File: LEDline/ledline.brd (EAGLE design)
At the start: 160 x 100 mm, 12 parts

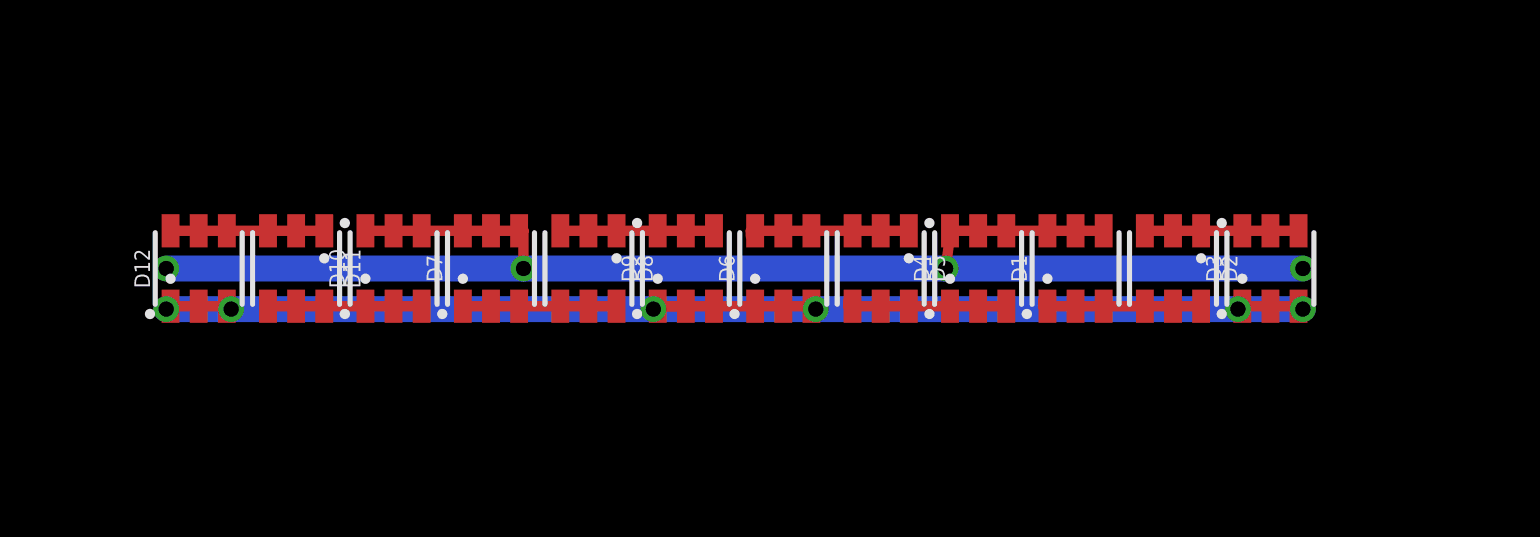
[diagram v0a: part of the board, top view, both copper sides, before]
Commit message: Heatsink and testpad added
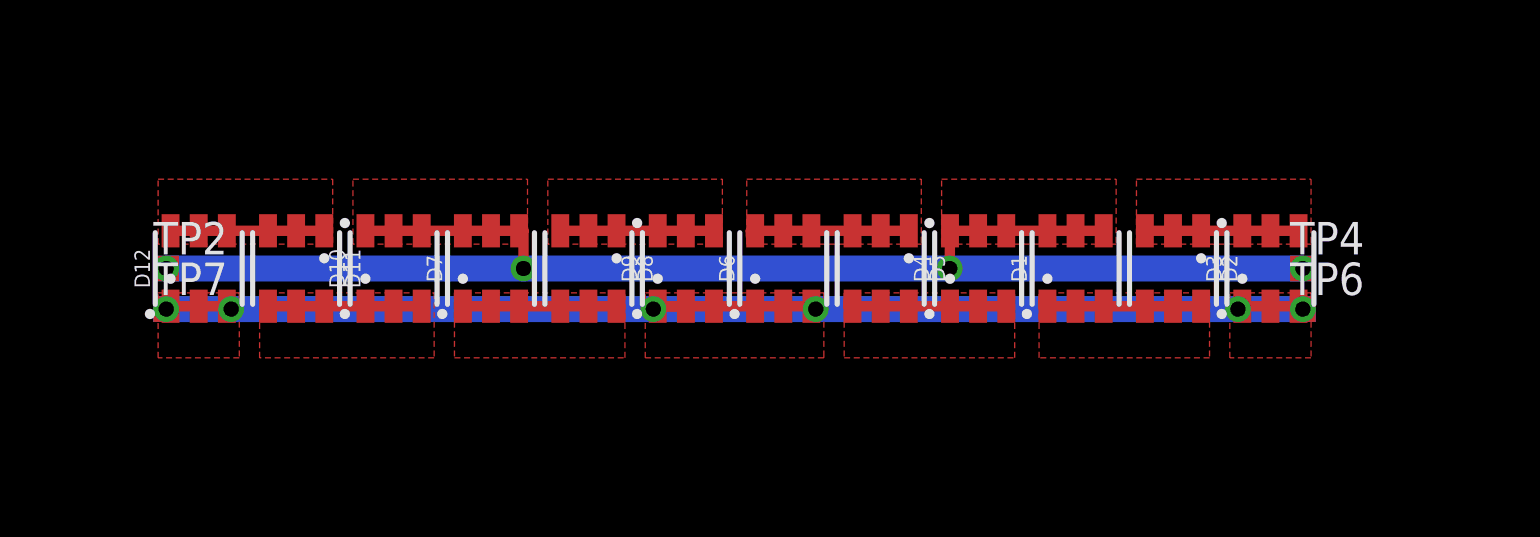
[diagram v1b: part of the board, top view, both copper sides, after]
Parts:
- added TP1, TP2, TP3, TP4, TP5, TP6, TP7, TP8: TPSQTP10SQ, testpad:TP10SQ
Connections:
- net GND: now also TP5.TP, TP6.TP, TP7.TP, TP8.TP
- net VCC: now also TP1.TP, TP2.TP, TP3.TP, TP4.TP
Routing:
- added copper zone on layer 1, net GND
- added copper zone on layer 1, net N$12
- added copper zone on layer 1, net N$13
- added copper zone on layer 1, net N$16
- added copper zone on layer 1, net N$17
- added copper zone on layer 1, net N$2
- added copper zone on layer 1, net N$4
- added copper zone on layer 1, net N$8
- added copper zone on layer 1, net N$9
- added copper zone on layer 1, net VCC
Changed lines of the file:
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@@
 <setting verticaltext="up"/>
 </settings>
-<grid distance="0.00625" unitdist="inch" unit="inch" style="lines" multiple="1" display="no" altdistance="0.025" altunitdist="inch" altunit="inch"/>
+<grid distance="0.00625" unitdist="inch" unit="mil" style="lines" multiple="1" display="no" altdistance="0.025" altunitdist="inch" altunit="inch"/>
 <layers>
 <layer number="1" name="Top" color="4" fill="1" visible="yes" active="yes"/>
@@
 <attribute name="PROD_ID" value="DIO-12113" x="46.99" y="77.47" size="1.778" layer="27" rot="R90" display="off"/>
 </element>
+<element name="TP2" library="testpad" package="TP10SQ" value="TPSQTP10SQ" x="26.67" y="77.47">
+<attribute name="TP_SIGNAL_NAME" value="" x="26.67" y="77.47" size="1.778" layer="27" display="off"/>
+</element>
+<element name="TP1" library="testpad" package="TP10SQ" value="TPSQTP10SQ" x="26.67" y="77.47" rot="MR0">
+<attribute name="TP_SIGNAL_NAME" value="" x="26.67" y="77.47" size="1.778" layer="28" rot="MR0" display="off"/>
+</element>
+<element name="TP3" library="testpad" package="TP10SQ" value="TPSQTP10SQ" x="71.12" y="77.47" rot="MR0">
+<attribute name="TP_SIGNAL_NAME" value="" x="71.12" y="77.47" size="1.778" layer="28" rot="MR0" display="off"/>
+</element>
+<element name="TP4" library="testpad" package="TP10SQ" value="TPSQTP10SQ" x="71.12" y="77.47">
+<attribute name="TP_SIGNAL_NAME" value="" x="71.12" y="77.47" size="1.778" layer="27" display="off"/>
+</element>
+<element name="TP5" library="testpad" package="TP10SQ" value="TPSQTP10SQ" x="71.12" y="75.8825" rot="MR0">
+<attribute name="TP_SIGNAL_NAME" value="" x="71.12" y="75.8825" size="1.778" layer="28" rot="MR0" display="off"/>
+</element>
+<element name="TP6" library="testpad" package="TP10SQ" value="TPSQTP10SQ" x="71.12" y="75.8825">
+<attribute name="TP_SIGNAL_NAME" value="" x="71.12" y="75.8825" size="1.778" layer="27" display="off"/>
+</element>
+<element name="TP7" library="testpad" package="TP10SQ" value="TPSQTP10SQ" x="26.67" y="75.8825">
+<attribute name="TP_SIGNAL_NAME" value="" x="26.67" y="75.8825" size="1.778" layer="27" display="off"/>
+</element>
+<element name="TP8" library="testpad" package="TP10SQ" value="TPSQTP10SQ" x="26.67" y="75.8825" rot="MR0">
+<attribute name="TP_SIGNAL_NAME" value="" x="26.67" y="75.8825" size="1.778" layer="28" rot="MR0" display="off"/>
+</element>
 </elements>
 <signals>
@@
 <wire x1="61.13" y1="75.995" x2="60.96" y2="75.995" width="0.4064" layer="1"/>
 <wire x1="60.96" y1="75.995" x2="60.96" y2="76.2" width="0.4064" layer="1"/>
+<polygon width="0.3048" layer="1" thermals="no">
+<vertex x="60.80125" y="73.9775"/>
+<vertex x="60.80125" y="76.5175"/>
+<vertex x="67.46875" y="76.5175"/>
+<vertex x="67.46875" y="73.9775"/>
+</polygon>
 </signal>
 <signal name="N$4">
@@
 <wire x1="66.04" y1="78.945" x2="67.14" y2="78.945" width="0.4064" layer="1"/>
 <wire x1="69.85" y1="78.945" x2="68.75" y2="78.945" width="0.4064" layer="1"/>
+<polygon width="0.3048" layer="1" thermals="no">
+<vertex x="64.61125" y="78.4225"/>
+<vertex x="64.61125" y="80.9625"/>
+<vertex x="71.4375" y="80.9625"/>
+<vertex x="71.4375" y="78.4225"/>
+</polygon>
 </signal>
 <signal name="N$8">
@@
 <wire x1="53.51" y1="75.995" x2="53.34" y2="75.995" width="0.4064" layer="1"/>
 <wire x1="53.34" y1="75.995" x2="53.34" y2="76.2" width="0.4064" layer="1"/>
+<polygon width="0.3048" layer="1" thermals="no">
+<vertex x="53.18125" y="76.5175"/>
+<vertex x="53.18125" y="73.9775"/>
+<vertex x="59.84875" y="73.9775"/>
+<vertex x="59.84875" y="76.5175"/>
+</polygon>
 </signal>
 <signal name="N$9">
@@
 <wire x1="49.7" y1="78.945" x2="49.53" y2="78.945" width="0.4064" layer="1"/>
 <wire x1="49.53" y1="78.945" x2="49.53" y2="78.74" width="0.4064" layer="1"/>
+<polygon width="0.3048" layer="1" thermals="no">
+<vertex x="49.37125" y="78.4225"/>
+<vertex x="49.37125" y="80.9625"/>
+<vertex x="56.1975" y="80.9625"/>
+<vertex x="56.1975" y="78.4225"/>
+</polygon>
 </signal>
 <signal name="N$12">
@@
 <wire x1="43.18" y1="75.995" x2="42.08" y2="75.995" width="0.4064" layer="1"/>
 <wire x1="39.37" y1="75.995" x2="40.47" y2="75.995" width="0.4064" layer="1"/>
+<polygon width="0.3048" layer="1" thermals="no">
+<vertex x="37.94125" y="76.5175"/>
+<vertex x="37.94125" y="73.9775"/>
+<vertex x="44.60875" y="73.9775"/>
+<vertex x="44.60875" y="76.5175"/>
+</polygon>
 </signal>
 <signal name="N$13">
@@
 <wire x1="46.99" y1="78.945" x2="48.09" y2="78.945" width="0.4064" layer="1"/>
 <wire x1="46.99" y1="78.945" x2="45.89" y2="78.945" width="0.4064" layer="1"/>
+<polygon width="0.3048" layer="1" thermals="no">
+<vertex x="41.5925" y="78.4225"/>
+<vertex x="41.5925" y="80.9625"/>
+<vertex x="48.41875" y="80.9625"/>
+<vertex x="48.41875" y="78.4225"/>
+</polygon>
 </signal>
 <signal name="N$16">
@@
 <wire x1="30.65" y1="75.995" x2="31.75" y2="75.995" width="0.4064" layer="1"/>
 <wire x1="31.75" y1="75.995" x2="31.75" y2="76.2" width="0.4064" layer="1"/>
+<polygon width="0.3048" layer="1" thermals="no">
+<vertex x="30.32125" y="73.9775"/>
+<vertex x="30.32125" y="76.5175"/>
+<vertex x="37.1475" y="76.5175"/>
+<vertex x="37.1475" y="73.9775"/>
+</polygon>
 </signal>
 <signal name="N$17">
@@
 <wire x1="32.85" y1="78.945" x2="31.75" y2="78.945" width="0.4064" layer="1"/>
 <wire x1="31.75" y1="78.945" x2="31.75" y2="78.74" width="0.4064" layer="1"/>
+<polygon width="0.3048" layer="1" thermals="no">
+<vertex x="26.3525" y="78.4225"/>
+<vertex x="26.3525" y="80.9625"/>
+<vertex x="33.17875" y="80.9625"/>
+<vertex x="33.17875" y="78.4225"/>
+</polygon>
 </signal>
 <signal name="VCC">
@@
 <wire x1="40.64" y1="78.945" x2="40.64" y2="77.47" width="0.4064" layer="1"/>
 <via x="40.64" y="77.47" extent="1-16" drill="0.6" shape="square"/>
-<wire x1="40.64" y1="77.47" x2="57.15" y2="77.47" width="1.016" layer="16"/>
-<via x="57.15" y="77.47" extent="1-16" drill="0.6" shape="square"/>
-<wire x1="57.15" y1="77.47" x2="57.32" y2="78.74" width="0.4064" layer="1"/>
+<wire x1="40.64" y1="77.47" x2="57.30875" y2="77.47" width="1.016" layer="16"/>
+<via x="57.30875" y="77.47" extent="1-16" drill="0.6" shape="square"/>
+<wire x1="57.30875" y1="77.47" x2="57.32" y2="78.74" width="0.4064" layer="1"/>
 <wire x1="57.32" y1="78.74" x2="57.32" y2="78.945" width="0.4064" layer="1"/>
 <wire x1="62.23" y1="78.945" x2="63.33" y2="78.945" width="0.4064" layer="1"/>
@@
 <wire x1="58.42" y1="78.945" x2="59.52" y2="78.945" width="0.4064" layer="1"/>
 <wire x1="40.64" y1="77.47" x2="26.67" y2="77.47" width="1.016" layer="16"/>
-<wire x1="57.15" y1="77.47" x2="71.12" y2="77.47" width="1.016" layer="16"/>
+<wire x1="57.30875" y1="77.47" x2="71.12" y2="77.47" width="1.016" layer="16"/>
 <via x="71.12" y="77.47" extent="1-16" drill="0.6" shape="square"/>
 <via x="26.67" y="77.47" extent="1-16" drill="0.6" shape="square"/>
+<contactref element="TP2" pad="TP"/>
+<contactref element="TP1" pad="TP"/>
+<contactref element="TP3" pad="TP"/>
+<contactref element="TP4" pad="TP"/>
+<polygon width="0.3048" layer="1" thermals="no">
+<vertex x="56.99125" y="78.4225"/>
+<vertex x="56.99125" y="80.9625"/>
+<vertex x="63.8175" y="80.9625"/>
+<vertex x="63.8175" y="78.4225"/>
+</polygon>
+<polygon width="0.3048" layer="1" thermals="no">
+<vertex x="33.9725" y="78.4225"/>
+<vertex x="33.9725" y="80.9625"/>
+<vertex x="40.79875" y="80.9625"/>
+<vertex x="40.79875" y="78.4225"/>
+</polygon>
 </signal>
 <signal name="GND">
@@
 <wire x1="29.21" y1="75.8825" x2="26.67" y2="75.8825" width="1.016" layer="16"/>
 <via x="26.67" y="75.8825" extent="1-16" drill="0.6" shape="square"/>
+<contactref element="TP8" pad="TP"/>
+<contactref element="TP7" pad="TP"/>
+<contactref element="TP6" pad="TP"/>
+<contactref element="TP5" pad="TP"/>
+<polygon width="0.3048" layer="1" thermals="no">
+<vertex x="26.3525" y="73.9775"/>
+<vertex x="26.3525" y="76.5175"/>
+<vertex x="29.5275" y="76.5175"/>
+<vertex x="29.5275" y="73.9775"/>
+</polygon>
+<polygon width="0.3048" layer="1" thermals="no">
+<vertex x="45.4025" y="73.9775"/>
+<vertex x="45.4025" y="76.5175"/>
+<vertex x="52.3875" y="76.5175"/>
+<vertex x="52.3875" y="74.13625"/>
+<vertex x="52.3875" y="73.9775"/>
+</polygon>
+<polygon width="0.3048" layer="1" thermals="no">
+<vertex x="68.2625" y="73.9775"/>
+<vertex x="68.2625" y="76.5175"/>
+<vertex x="71.4375" y="76.5175"/>
+<vertex x="71.4375" y="73.9775"/>
+</polygon>
 </signal>
 </signals>

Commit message: MOAAAAR heatsink
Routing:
- net VCC: track 59.6 -> 56.8 mm, vias 4 -> 6
- net N$9: vias 0 -> 2
- net N$4: vias 0 -> 2
- net N$17: vias 0 -> 2
- net N$13: vias 0 -> 2
- added copper zone on layer 16, net GND
- added copper zone on layer 16, net N$13
- added copper zone on layer 16, net N$17
- added copper zone on layer 16, net N$4
- added copper zone on layer 16, net N$9
- added copper zone on layer 16, net VCC
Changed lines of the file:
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@@
 <layer number="27" name="tValues" color="7" fill="1" visible="no" active="yes"/>
 <layer number="28" name="bValues" color="7" fill="1" visible="no" active="yes"/>
-<layer number="29" name="tStop" color="7" fill="3" visible="no" active="yes"/>
-<layer number="30" name="bStop" color="7" fill="6" visible="no" active="yes"/>
+<layer number="29" name="tStop" color="7" fill="3" visible="yes" active="yes"/>
+<layer number="30" name="bStop" color="7" fill="6" visible="yes" active="yes"/>
 <layer number="31" name="tCream" color="7" fill="4" visible="no" active="yes"/>
 <layer number="32" name="bCream" color="7" fill="5" visible="no" active="yes"/>
@@
 <wire x1="160" y1="100" x2="0" y2="100" width="0" layer="20"/>
 <wire x1="0" y1="100" x2="0" y2="0" width="0" layer="20"/>
+<polygon width="0.3048" layer="29">
+<vertex x="26.3525" y="73.9775"/>
+<vertex x="29.5275" y="73.9775"/>
+<vertex x="29.5275" y="74.93"/>
+<vertex x="26.3525" y="74.93"/>
+</polygon>
+<polygon width="0.3048" layer="30">
+<vertex x="26.3525" y="74.93"/>
+<vertex x="26.3525" y="73.9775"/>
+<vertex x="29.5275" y="73.9775"/>
+<vertex x="29.5275" y="74.93"/>
+</polygon>
+<polygon width="0.3048" layer="29">
+<vertex x="68.2625" y="73.9775"/>
+<vertex x="71.4375" y="73.9775"/>
+<vertex x="71.4375" y="74.93"/>
+<vertex x="68.2625" y="74.93"/>
+</polygon>
+<polygon width="0.3048" layer="30">
+<vertex x="68.2625" y="74.93"/>
+<vertex x="68.2625" y="73.9775"/>
+<vertex x="71.4375" y="73.9775"/>
+<vertex x="71.4375" y="74.93"/>
+</polygon>
+<polygon width="0.3048" layer="29">
+<vertex x="63.8175" y="80.9625"/>
+<vertex x="56.99125" y="80.9625"/>
+<vertex x="56.99125" y="80.16875"/>
+<vertex x="63.8175" y="80.16875"/>
+</polygon>
+<polygon width="0.3048" layer="30">
+<vertex x="56.99125" y="80.9625"/>
+<vertex x="56.99125" y="80.16875"/>
+<vertex x="63.8175" y="80.16875"/>
+<vertex x="63.8175" y="80.9625"/>
+</polygon>
+<polygon width="0.3048" layer="29">
+<vertex x="33.9725" y="80.9625"/>
+<vertex x="33.9725" y="80.16875"/>
+<vertex x="40.79875" y="80.16875"/>
+<vertex x="40.79875" y="80.9625"/>
+</polygon>
+<polygon width="0.3048" layer="30">
+<vertex x="33.9725" y="80.9625"/>
+<vertex x="33.9725" y="80.16875"/>
+<vertex x="40.79875" y="80.16875"/>
+<vertex x="40.79875" y="80.9625"/>
+</polygon>
 </plain>
 <attributes>
@@
 <vertex x="71.4375" y="78.4225"/>
 </polygon>
+<polygon width="0.3048" layer="16" thermals="no">
+<vertex x="64.61125" y="80.9625"/>
+<vertex x="64.61125" y="78.4225"/>
+<vertex x="71.4375" y="78.4225"/>
+<vertex x="71.4375" y="80.9625"/>
+</polygon>
+<via x="66.04" y="78.89875" extent="1-16" drill="0.6" shape="square"/>
+<via x="69.85" y="78.89875" extent="1-16" drill="0.6" shape="square"/>
 </signal>
 <signal name="N$8">
@@
 <vertex x="56.1975" y="78.4225"/>
 </polygon>
+<polygon width="0.3048" layer="16" thermals="no">
+<vertex x="49.37125" y="80.9625"/>
+<vertex x="56.1975" y="80.9625"/>
+<vertex x="56.1975" y="78.4225"/>
+<vertex x="49.37125" y="78.4225"/>
+</polygon>
+<via x="50.8" y="78.89875" extent="1-16" drill="0.6" shape="square"/>
+<via x="54.61" y="78.89875" extent="1-16" drill="0.6" shape="square"/>
 </signal>
 <signal name="N$12">
@@
 <vertex x="48.41875" y="78.4225"/>
 </polygon>
+<polygon width="0.3048" layer="16" thermals="no">
+<vertex x="41.5925" y="80.9625"/>
+<vertex x="41.5925" y="78.4225"/>
+<vertex x="48.41875" y="78.4225"/>
+<vertex x="48.41875" y="80.9625"/>
+</polygon>
+<via x="43.18" y="78.89875" extent="1-16" drill="0.6" shape="square"/>
+<via x="46.99" y="78.89875" extent="1-16" drill="0.6" shape="square"/>
 </signal>
 <signal name="N$16">
@@
 <wire x1="30.65" y1="78.945" x2="31.75" y2="78.945" width="0.4064" layer="1"/>
 <wire x1="32.85" y1="78.945" x2="31.75" y2="78.945" width="0.4064" layer="1"/>
-<wire x1="31.75" y1="78.945" x2="31.75" y2="78.74" width="0.4064" layer="1"/>
+<wire x1="31.75" y1="78.945" x2="31.75" y2="78.89875" width="0.4064" layer="1"/>
 <polygon width="0.3048" layer="1" thermals="no">
 <vertex x="26.3525" y="78.4225"/>
@@
 <vertex x="33.17875" y="78.4225"/>
 </polygon>
+<polygon width="0.3048" layer="16" thermals="no">
+<vertex x="26.3525" y="80.9625"/>
+<vertex x="33.17875" y="80.9625"/>
+<vertex x="33.17875" y="78.4225"/>
+<vertex x="26.3525" y="78.4225"/>
+</polygon>
+<wire x1="31.75" y1="78.89875" x2="31.75" y2="78.74" width="0.4064" layer="1"/>
+<via x="31.75" y="78.89875" extent="1-16" drill="0.6" shape="square"/>
+<via x="27.94" y="78.89875" extent="1-16" drill="0.6" shape="square"/>
 </signal>
 <signal name="VCC">
@@
 <wire x1="36.66" y1="78.945" x2="35.56" y2="78.945" width="0.4064" layer="1"/>
 <wire x1="40.47" y1="78.945" x2="40.64" y2="78.945" width="0.4064" layer="1"/>
-<wire x1="40.64" y1="78.945" x2="40.64" y2="77.47" width="0.4064" layer="1"/>
 <via x="40.64" y="77.47" extent="1-16" drill="0.6" shape="square"/>
 <wire x1="40.64" y1="77.47" x2="57.30875" y2="77.47" width="1.016" layer="16"/>
 <via x="57.30875" y="77.47" extent="1-16" drill="0.6" shape="square"/>
-<wire x1="57.30875" y1="77.47" x2="57.32" y2="78.74" width="0.4064" layer="1"/>
 <wire x1="57.32" y1="78.74" x2="57.32" y2="78.945" width="0.4064" layer="1"/>
 <wire x1="62.23" y1="78.945" x2="63.33" y2="78.945" width="0.4064" layer="1"/>
@@
 <contactref element="TP4" pad="TP"/>
 <polygon width="0.3048" layer="1" thermals="no">
-<vertex x="56.99125" y="78.4225"/>
+<vertex x="56.99125" y="77.1525"/>
 <vertex x="56.99125" y="80.9625"/>
 <vertex x="63.8175" y="80.9625"/>
-<vertex x="63.8175" y="78.4225"/>
-</polygon>
-<polygon width="0.3048" layer="1" thermals="no">
-<vertex x="33.9725" y="78.4225"/>
+<vertex x="63.8175" y="77.1525"/>
+</polygon>
+<polygon width="0.3048" layer="1" thermals="no">
+<vertex x="33.9725" y="77.1525"/>
 <vertex x="33.9725" y="80.9625"/>
 <vertex x="40.79875" y="80.9625"/>
-<vertex x="40.79875" y="78.4225"/>
-</polygon>
+<vertex x="40.79875" y="77.1525"/>
+</polygon>
+<polygon width="0.3048" layer="16" thermals="no">
+<vertex x="56.99125" y="80.9625"/>
+<vertex x="56.99125" y="77.1525"/>
+<vertex x="63.8175" y="77.1525"/>
+<vertex x="63.8175" y="80.9625"/>
+</polygon>
+<polygon width="0.3048" layer="16" thermals="no">
+<vertex x="33.9725" y="80.9625"/>
+<vertex x="33.9725" y="77.1525"/>
+<vertex x="40.79875" y="77.1525"/>
+<vertex x="40.79875" y="80.9625"/>
+</polygon>
+<via x="34.44875" y="77.47" extent="1-16" drill="0.6" shape="square"/>
+<via x="63.34125" y="77.47" extent="1-16" drill="0.6" shape="square"/>
 </signal>
 <signal name="GND">
@@
 <vertex x="71.4375" y="73.9775"/>
 </polygon>
-</signal>
+<polygon width="0.3048" layer="16" thermals="no">
+<vertex x="26.3525" y="76.5175"/>
+<vertex x="26.3525" y="73.9775"/>
+<vertex x="29.5275" y="73.9775"/>
+<vertex x="29.5275" y="76.5175"/>
+</polygon>
+<polygon width="0.3048" layer="16" thermals="no">
+<vertex x="68.2625" y="76.5175"/>
+<vertex x="68.2625" y="73.9775"/>
+<vertex x="71.4375" y="73.9775"/>
+<vertex x="71.4375" y="76.5175"/>
+</polygon>
+<polygon width="0.3048" layer="16" thermals="no">
+<vertex x="45.4025" y="76.5175"/>
+<vertex x="45.4025" y="73.9775"/>
+<vertex x="52.3875" y="73.9775"/>
+<vertex x="52.3875" y="76.5175"/>
+</polygon>
+</signal>
